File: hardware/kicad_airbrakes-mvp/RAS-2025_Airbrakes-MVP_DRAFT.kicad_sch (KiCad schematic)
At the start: 12 parts, among them M1 FeatherS3 ESP32, M1 Motor_Servo, SW1 Screw_Switch

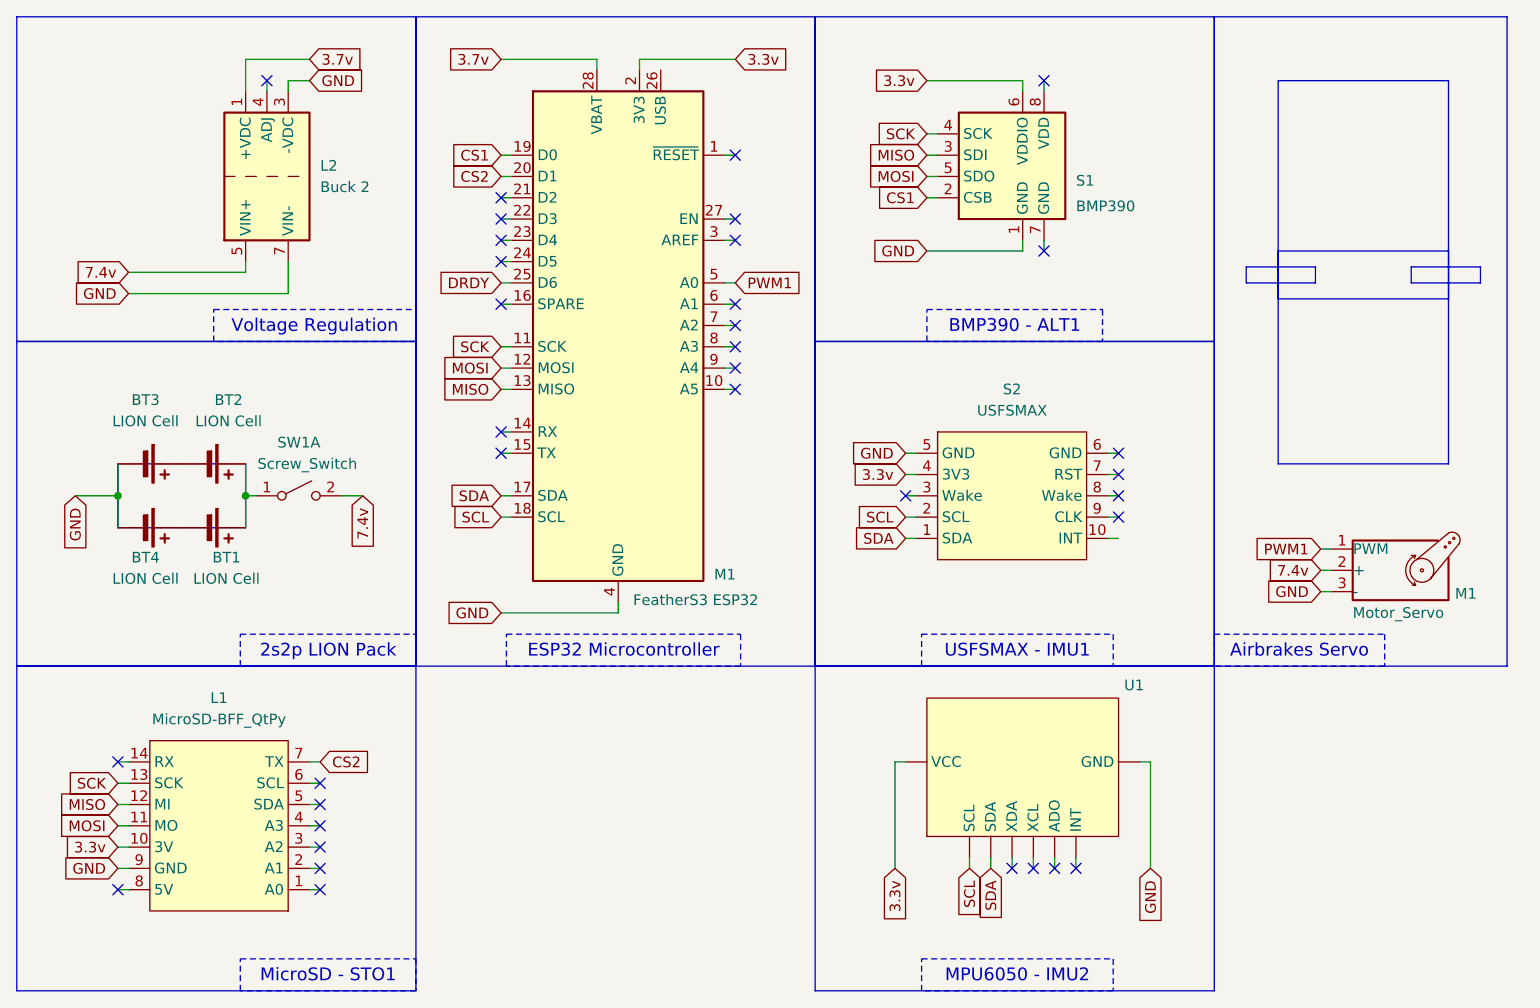
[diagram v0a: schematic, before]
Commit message: Updates the airbrake schematic
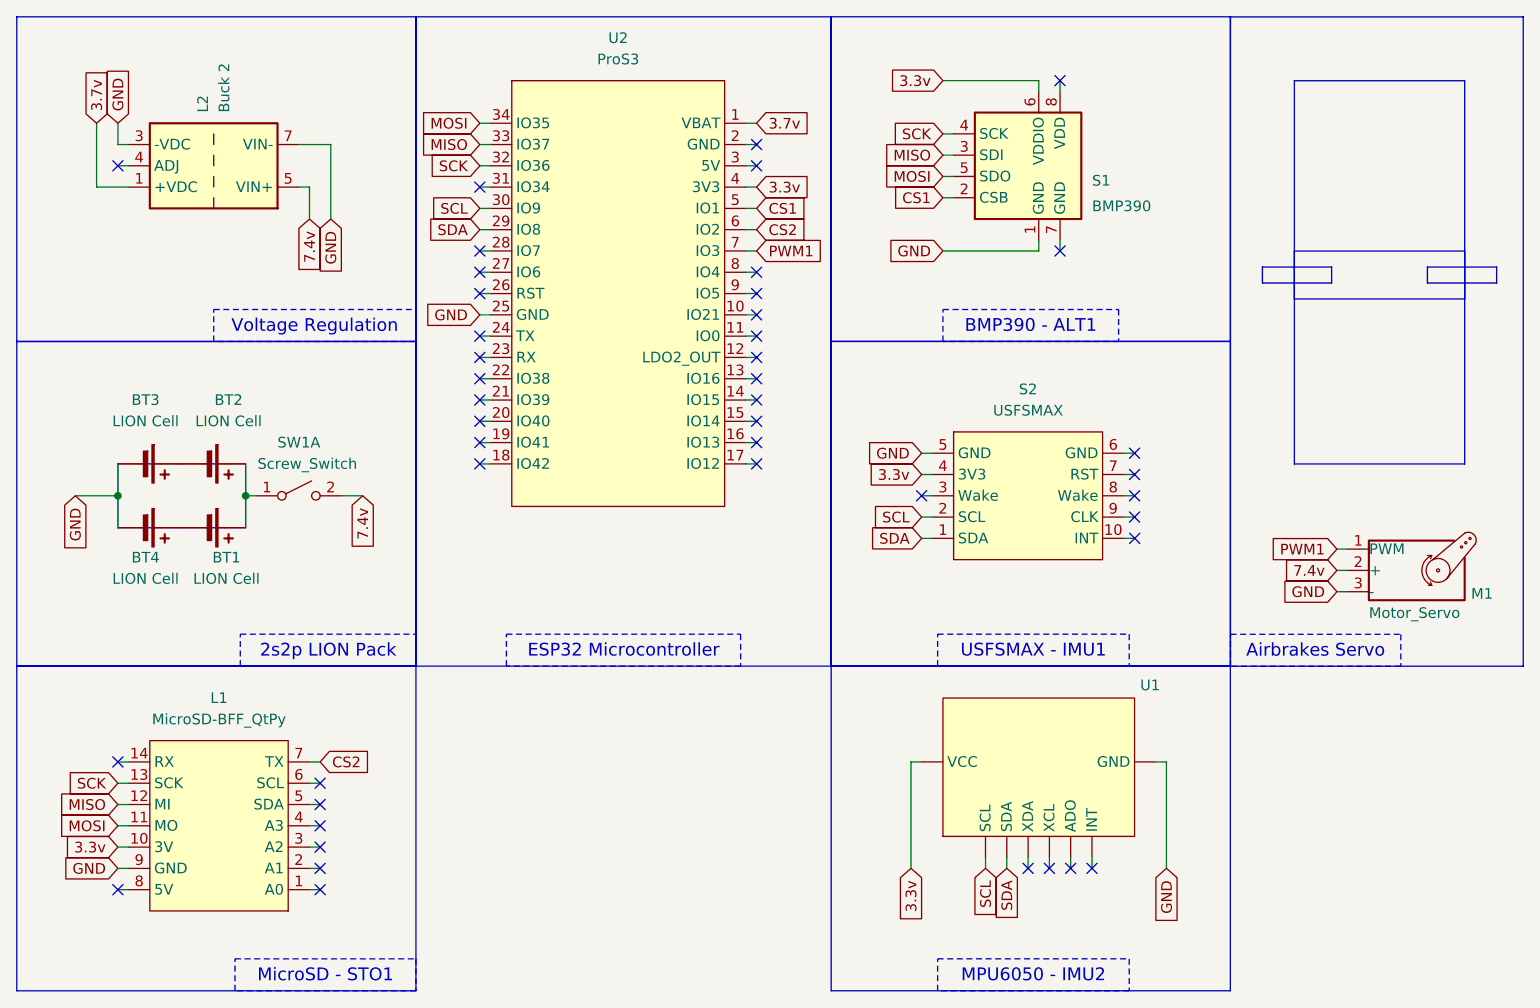
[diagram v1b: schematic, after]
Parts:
- removed M1: FeatherS3 ESP32, Module:Adafruit_Feather, symbol MCU_Module:Adafruit_Feather_ESP32-S3_MM
- added U2: ProS3, symbol custom-ras-symbols:ProS3
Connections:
- net 3.3v: now also U2.4 (3V3)
- net 3.7v: now also U2.1 (VBAT)
- net CS1: now also U2.5 (IO1)
- net CS2: now also U2.6 (IO2)
- net GND: now also U2.25 (GND)
- net MISO: now also U2.33 (IO37)
- net MOSI: now also U2.34 (IO35)
- net PWM1: now also U2.7 (IO3)
- net SCK: now also U2.32 (IO36)
- net SCL: now also U2.30 (IO9)
- net SDA: now also U2.29 (IO8)
- no-connect marks 35 -> 44
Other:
- moved on the sheet: L2, M1, S1, S2, U1
